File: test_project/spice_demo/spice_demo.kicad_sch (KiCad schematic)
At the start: 5 parts

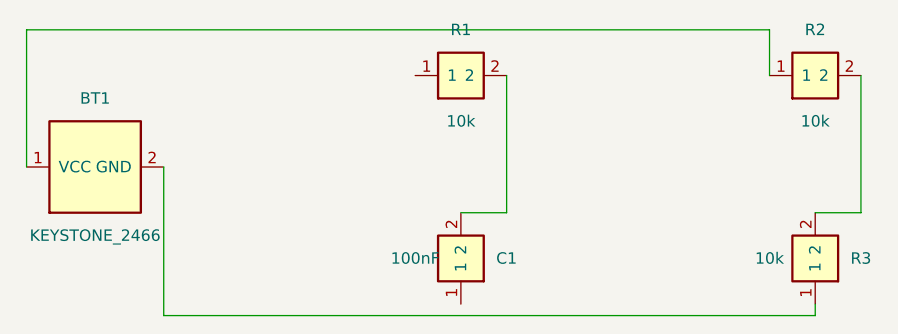
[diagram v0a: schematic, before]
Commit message: chore: no_connect pin type, demo tweaks, GUI wire_test reference
- parser.py / symbol.py: allow 'no_connect' pin electrical type
- test_project flashlight/spice demo + e2e test minor updates; regenerated
  spice_demo / dangling_test fixtures
- add test_project/wire_test (GUI-drawn 2-resistor + bare-wire reference) — the
  ground-truth artifact that isolated the missing-instances-block bug

Co-Authored-By: Claude Opus 4.8 (1M context) <noreply@anthropic.com>
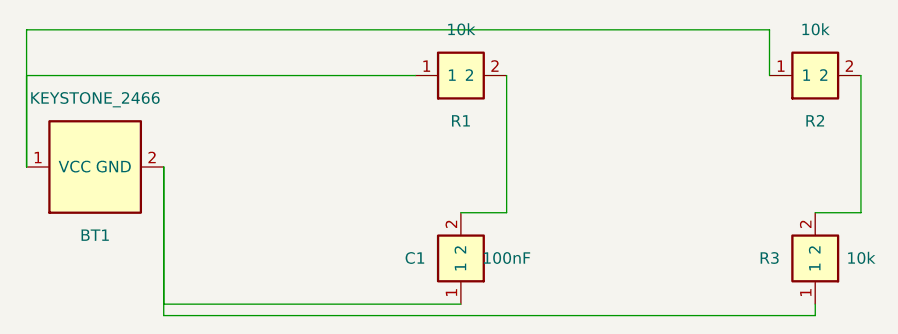
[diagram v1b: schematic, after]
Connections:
- net at R1.1: now also BT1.1 (VCC), R2.1
- net at BT1.2 (GND), R3.1: now also C1.1
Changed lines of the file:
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@@
 	(paper "A4" portrait)
 	(symbol
-		(lib_id spice_demo:KEYSTONE_2466)
+		(lib_id "spice_demo:KEYSTONE_2466")
 		(at 69.850 80.010 0.0)
 		(unit 1)
@@
 		(on_board yes)
 		(property "Reference" "BT1"
-			(at 69.850 72.390 0.0)
+			(at 69.850 87.630 0.0)
 			(effects (font (size 1.27 1.27)))
 		)
 		(property "Value" "KEYSTONE_2466"
-			(at 69.850 87.630 0.0)
+			(at 69.850 72.390 0.0)
 			(effects (font (size 1.27 1.27)))
 		)
@@
 	)
 	(symbol
-		(lib_id spice_demo:R)
+		(lib_id "spice_demo:R")
 		(at 110.490 69.850 0.0)
 		(unit 1)
@@
 		(on_board yes)
 		(property "Reference" "R1"
-			(at 110.490 64.770 0.0)
+			(at 110.490 74.930 0.0)
 			(effects (font (size 1.27 1.27)))
 		)
 		(property "Value" "10k"
-			(at 110.490 74.930 0.0)
+			(at 110.490 64.770 0.0)
 			(effects (font (size 1.27 1.27)))
 		)
@@
 	)
 	(symbol
-		(lib_id spice_demo:C)
+		(lib_id "spice_demo:C")
 		(at 110.490 90.170 90.0)
 		(unit 1)
@@
 		(on_board yes)
 		(property "Reference" "C1"
-			(at 115.570 90.170 90.0)
+			(at 105.410 90.170 90.0)
 			(effects (font (size 1.27 1.27)))
 		)
 		(property "Value" "100nF"
-			(at 105.410 90.170 90.0)
+			(at 115.570 90.170 90.0)
 			(effects (font (size 1.27 1.27)))
 		)
@@
 	)
 	(symbol
-		(lib_id spice_demo:R)
+		(lib_id "spice_demo:R")
 		(at 149.860 69.850 0.0)
 		(unit 1)
@@
 		(on_board yes)
 		(property "Reference" "R2"
-			(at 149.860 64.770 0.0)
+			(at 149.860 74.930 0.0)
 			(effects (font (size 1.27 1.27)))
 		)
 		(property "Value" "10k"
-			(at 149.860 74.930 0.0)
+			(at 149.860 64.770 0.0)
 			(effects (font (size 1.27 1.27)))
 		)
@@
 	)
 	(symbol
-		(lib_id spice_demo:R)
+		(lib_id "spice_demo:R")
 		(at 149.860 90.170 90.0)
 		(unit 1)
@@
 		(on_board yes)
 		(property "Reference" "R3"
-			(at 154.940 90.170 90.0)
+			(at 144.780 90.170 90.0)
 			(effects (font (size 1.27 1.27)))
 		)
 		(property "Value" "10k"
-			(at 144.780 90.170 90.0)
+			(at 154.940 90.170 90.0)
 			(effects (font (size 1.27 1.27)))
 		)
@@
 		)
 	)
+	(wire (pts (xy 62.230 80.010) (xy 62.230 69.850)) (stroke (width 0) (type default)))
+	(wire (pts (xy 62.230 69.850) (xy 105.410 69.850)) (stroke (width 0) (type default)))
 	(wire (pts (xy 115.570 69.850) (xy 115.570 85.090)) (stroke (width 0) (type default)))
 	(wire (pts (xy 115.570 85.090) (xy 110.490 85.090)) (stroke (width 0) (type default)))
+	(wire (pts (xy 110.490 95.250) (xy 77.470 95.250)) (stroke (width 0) (type default)))
+	(wire (pts (xy 77.470 95.250) (xy 77.470 80.010)) (stroke (width 0) (type default)))
 	(wire (pts (xy 62.230 80.010) (xy 62.230 64.770)) (stroke (width 0) (type default)))
 	(wire (pts (xy 62.230 64.770) (xy 144.780 64.770)) (stroke (width 0) (type default)))
